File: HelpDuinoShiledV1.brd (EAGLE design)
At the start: 68 x 59.7 mm, 31 parts

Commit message: adding traces
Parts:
- removed LSP10, LSP11, LSP12, LSP14, LSP15, LSP16, LSP17, LSP18, LSP19, LSP20, LSP21, LSP22, LSP23, LSP5, LSP6, LSP7, LSP8, LSP9: SE13, solpad:SE13
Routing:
- net D6: track 18.6 -> 115.3 mm, vias 0 -> 4
- net D5: track 21.2 -> 114.2 mm, vias 0 -> 4
- net D11: track 24.3 -> 88.8 mm, vias 0 -> 4
- net D9: track 18.4 -> 75.3 mm, vias 0 -> 2
- net D12: track 15.6 -> 71.2 mm, vias 2 -> 5
- net D13: track 17.4 -> 72.2 mm, vias 0 -> 3
- net D10: track 19.3 -> 73.6 mm, vias 0 -> 2
- net D4: track 23.6 -> 71.9 mm, vias 0 -> 2
- net D8: track 39.1 -> 86.3 mm, vias 1 -> 5
- net D7: track 38.5 -> 81.2 mm, vias 1 -> 5
- net D3: track 83.8 -> 126.5 mm, vias 4 -> 6
- net D2: track 87.4 -> 118.5 mm, vias 0 -> 1
- net D1: track 47.7 -> 75.9 mm, vias 2 -> 3
- added copper zone on layer 1, net 5V

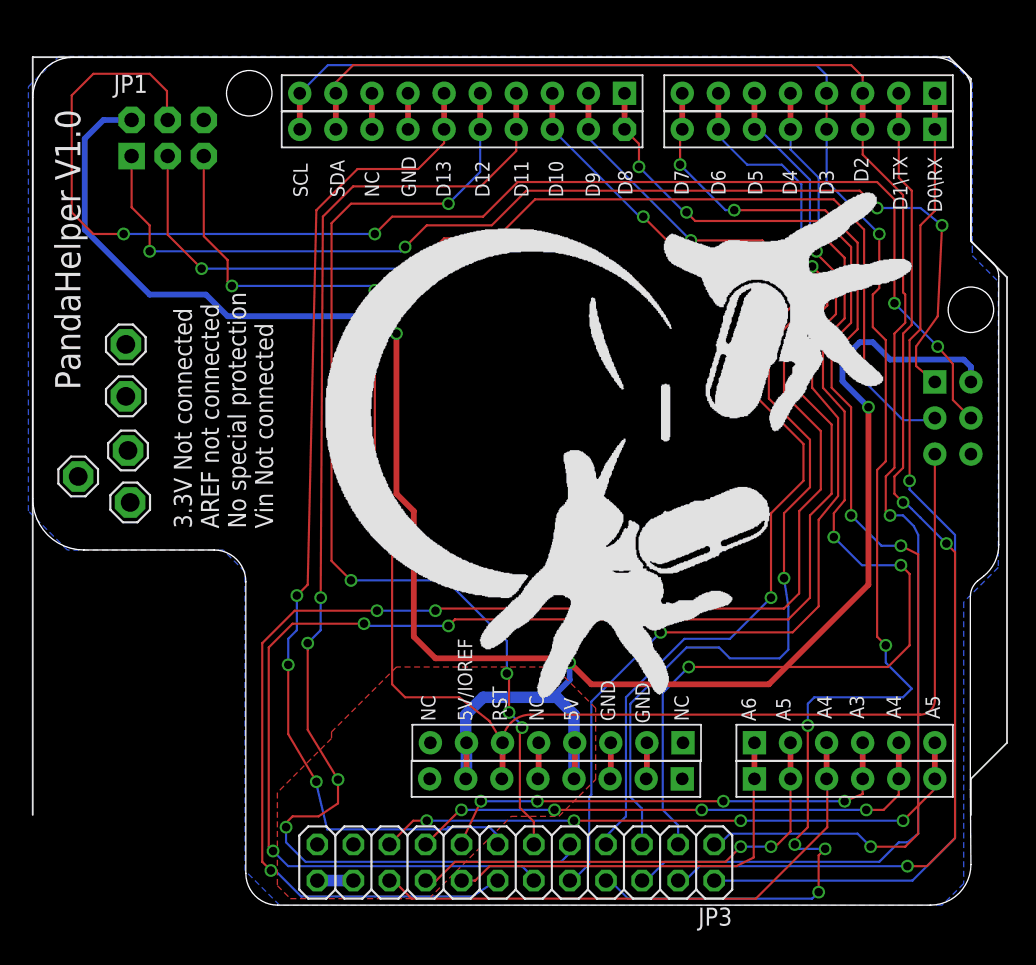
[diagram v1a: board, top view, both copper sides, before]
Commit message: added 3.3v
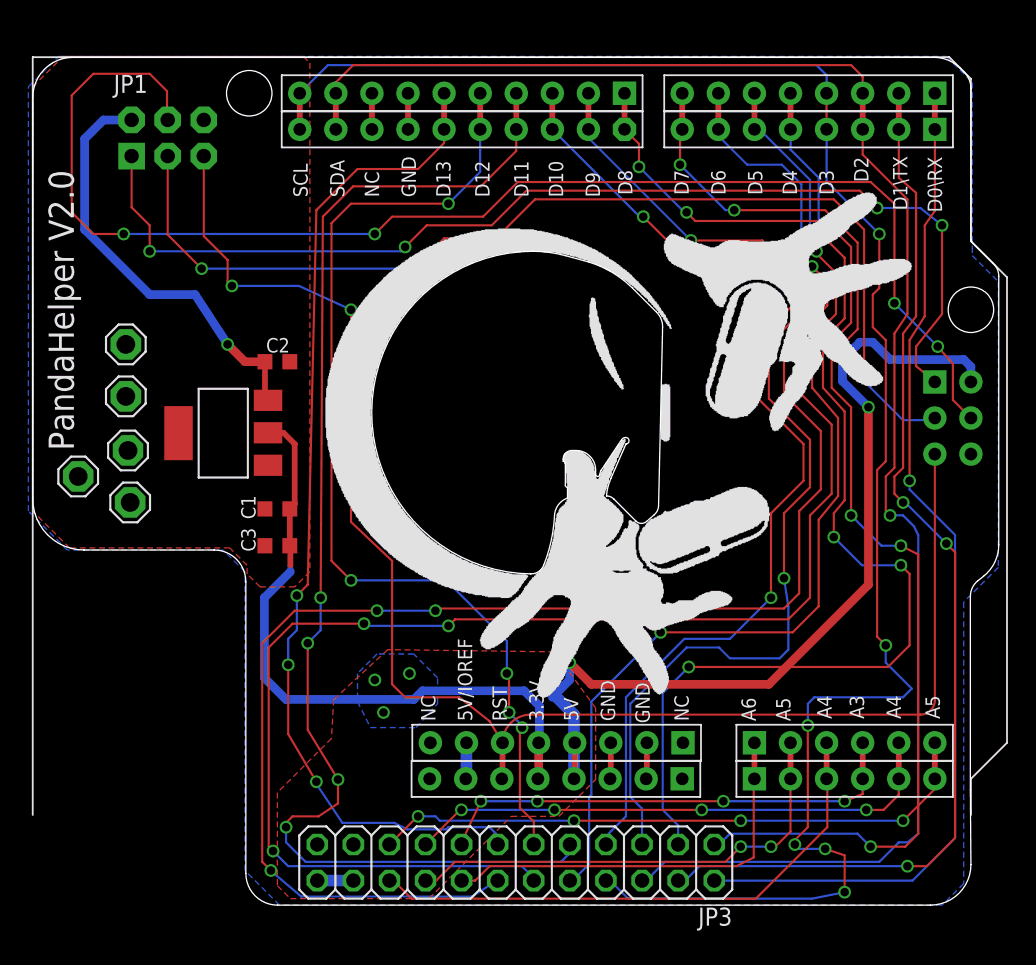
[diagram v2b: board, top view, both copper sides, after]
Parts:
- added C1: 4.7uF, rcl:C0603K
- added C2, C3: .1uf, rcl:C0603K
- added IC1: REG1117, burr-brown:SOT223
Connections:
- new net 3.3V: C1.1, C3.1, IC1.2
- net 5V: now also C2.1, IC1.3
- net GND: now also C1.2, C2.2, C3.2, IC1.1
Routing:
- net 5V: track 150.0 -> 99.9 mm, vias 3 -> 6
- net N$2: track 0.00 -> 32.3 mm
- net 3.3V: track 0.00 -> 9.51 mm
- net D3: track 126.5 -> 129.0 mm
- net RST: track 109.6 -> 107.5 mm
- net N$1: track 0.00 -> 1.07 mm
- net D13: track 72.2 -> 71.2 mm
- added copper zone on layer 16, net 5V
- added copper zone on layer 1, net GND
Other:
- outline, holes or cut-outs redrawn
- board text added: "3.3V"
- board text added: "PandaHelper V2.0"
- board text removed: "3.3V Not connected AREF not connected No special protection Vin Not connected"
- board text removed: "PandaHelper V1.0"
